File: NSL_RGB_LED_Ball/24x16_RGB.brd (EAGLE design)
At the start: 46.4 x 123.7 mm, 104 parts, among them IC1 MEGA8-AI, IC2 TLC5947XLP, IC3 TLC5947XLP, IC4 TLC5947XLP, IC5 MCP73123, IC6 BLUETOOTH-RN41", IC7 MMA7455L, IC8 OPA344, Q1 BSH201, X1 16Mhz

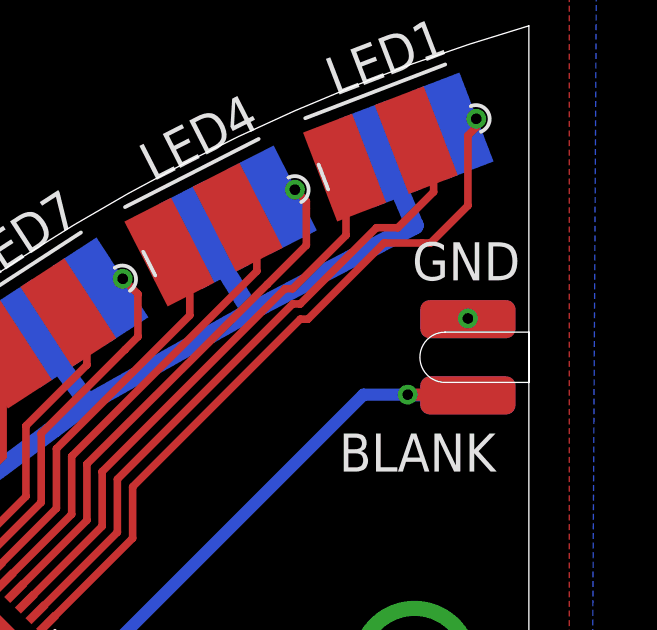
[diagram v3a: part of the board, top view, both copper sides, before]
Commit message: 
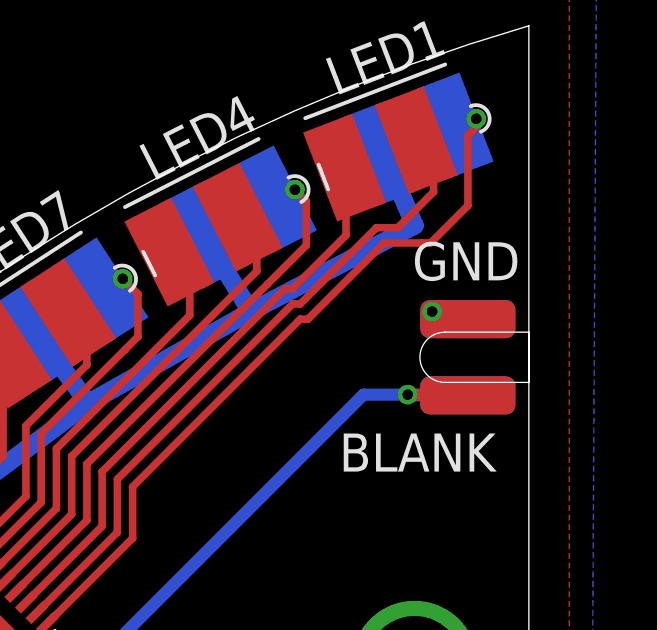
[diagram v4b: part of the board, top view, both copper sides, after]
